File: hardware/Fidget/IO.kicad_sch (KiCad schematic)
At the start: 8 parts

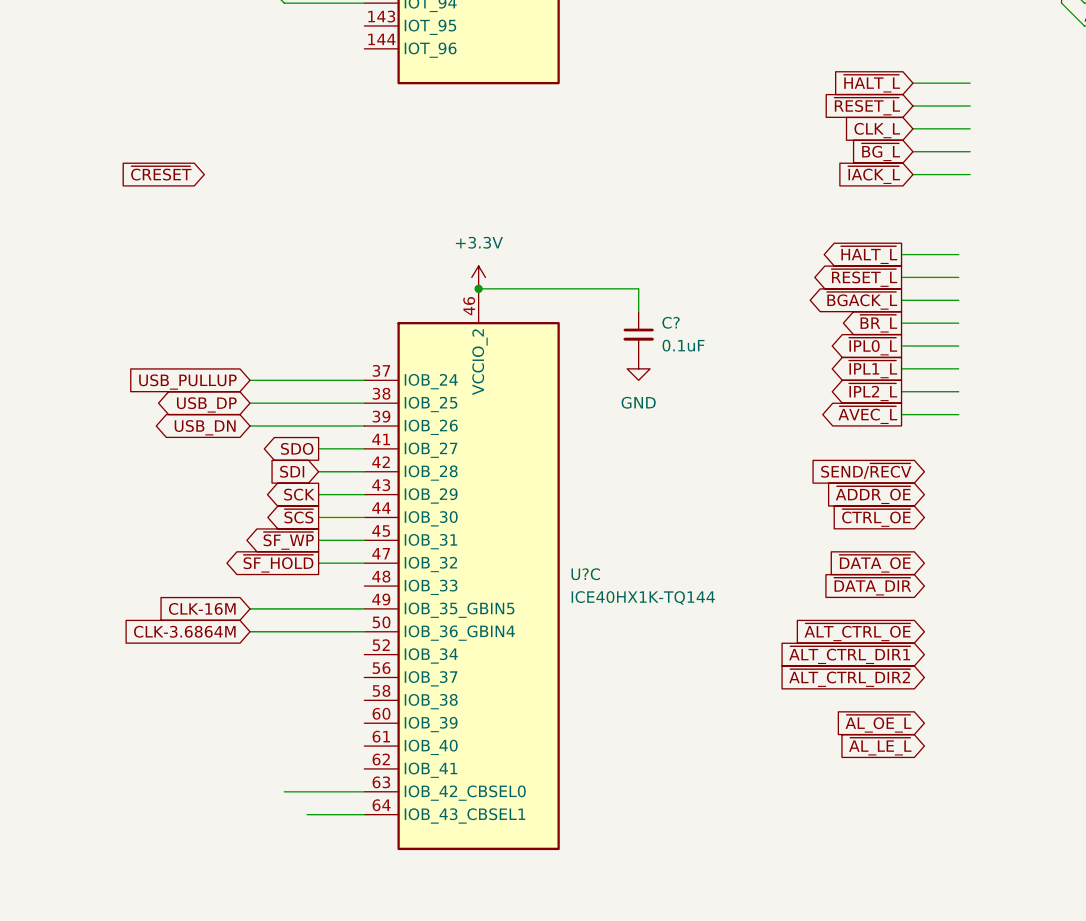
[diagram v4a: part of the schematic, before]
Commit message: Filled in more details in schematic
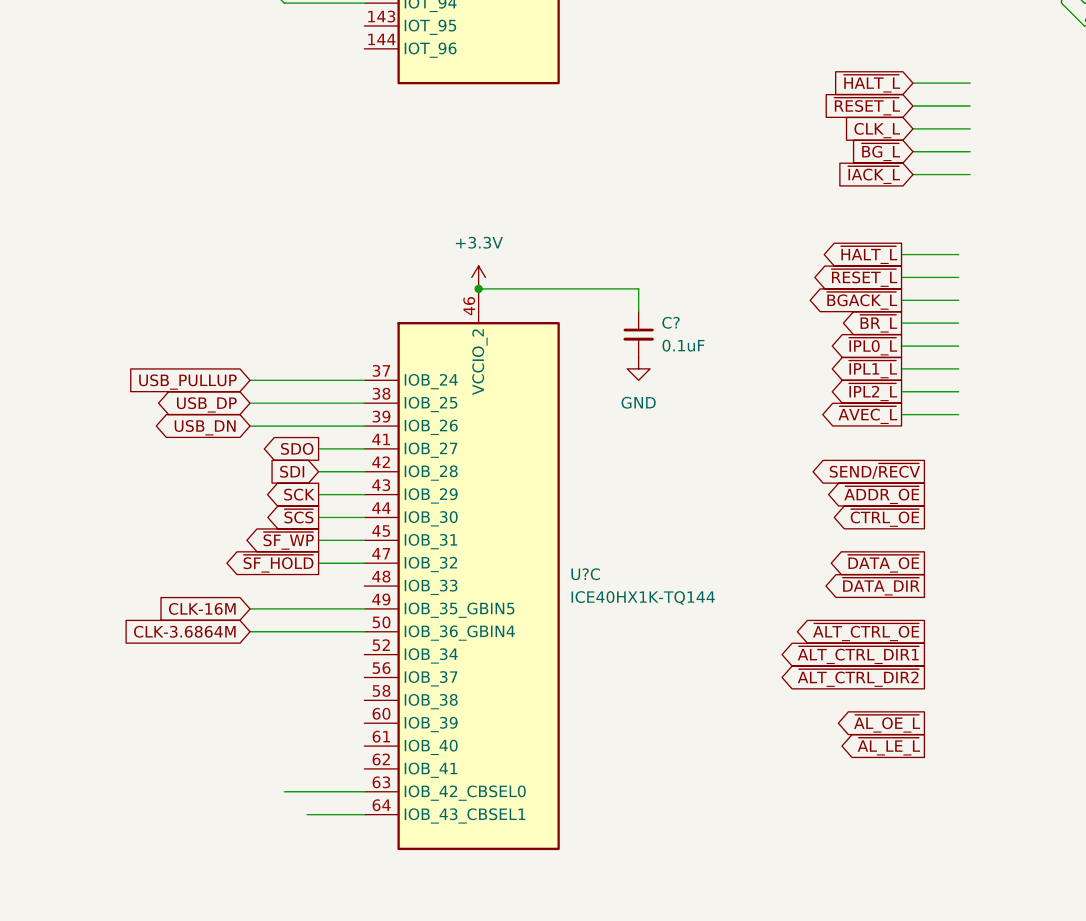
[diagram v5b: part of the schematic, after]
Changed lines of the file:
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@@
     (effects (font (size 1.27 1.27)) (justify left bottom))
   )
-  (global_label "~{DATA_DIR}" (shape input) (at 116.84 149.86 180) (fields_autoplaced)
+  (global_label "~{DATA_DIR}" (shape output) (at 116.84 149.86 180) (fields_autoplaced)
     (effects (font (size 1.27 1.27)) (justify right))
     (property "Intersheet References" "${INTERSHEET_REFS}" (id 0) (at 105.8998 149.7806 0)
@@
     )
   )
-  (global_label "~{AL_OE_L}" (shape input) (at 116.84 165.1 180) (fields_autoplaced)
+  (global_label "~{AL_OE_L}" (shape output) (at 116.84 165.1 180) (fields_autoplaced)
     (effects (font (size 1.27 1.27)) (justify right))
     (property "Intersheet References" "${INTERSHEET_REFS}" (id 0) (at 106.8674 165.0206 0)
@@
     )
   )
-  (global_label "~{DATA_OE}" (shape input) (at 116.84 147.32 180) (fields_autoplaced)
+  (global_label "~{DATA_OE}" (shape output) (at 116.84 147.32 180) (fields_autoplaced)
     (effects (font (size 1.27 1.27)) (justify right))
     (property "Intersheet References" "${INTERSHEET_REFS}" (id 0) (at 106.565 147.2406 0)
@@
     )
   )
-  (global_label "~{ALT_CTRL_DIR2}" (shape input) (at 116.84 160.02 180) (fields_autoplaced)
+  (global_label "~{ALT_CTRL_DIR2}" (shape output) (at 116.84 160.02 180) (fields_autoplaced)
     (effects (font (size 1.27 1.27)) (justify right))
     (property "Intersheet References" "${INTERSHEET_REFS}" (id 0) (at 100.5174 159.9406 0)
@@
     )
   )
-  (global_label "~{CRESET}" (shape input) (at 36.83 104.14 180) (fields_autoplaced)
-    (effects (font (size 1.27 1.27)) (justify right))
-    (property "Intersheet References" "${INTERSHEET_REFS}" (id 0) (at 27.4017 104.0606 0)
-      (effects (font (size 1.27 1.27)) (justify right) hide)
-    )
-  )
   (global_label "~{DS_L}" (shape input) (at 114.3 55.88 180) (fields_autoplaced)
     (effects (font (size 1.27 1.27)) (justify right))
@@
     )
   )
-  (global_label "~{ALT_CTRL_DIR1}" (shape input) (at 116.84 157.48 180) (fields_autoplaced)
+  (global_label "~{ALT_CTRL_DIR1}" (shape output) (at 116.84 157.48 180) (fields_autoplaced)
     (effects (font (size 1.27 1.27)) (justify right))
     (property "Intersheet References" "${INTERSHEET_REFS}" (id 0) (at 100.5174 157.4006 0)
@@
     )
   )
-  (global_label "~{AL_LE_L}" (shape input) (at 116.84 167.64 180) (fields_autoplaced)
+  (global_label "~{AL_LE_L}" (shape output) (at 116.84 167.64 180) (fields_autoplaced)
     (effects (font (size 1.27 1.27)) (justify right))
     (property "Intersheet References" "${INTERSHEET_REFS}" (id 0) (at 107.1698 167.5606 0)
@@
     )
   )
-  (global_label "SEND{slash}~{RECV}" (shape input) (at 116.84 137.16 180) (fields_autoplaced)
+  (global_label "SEND{slash}~{RECV}" (shape output) (at 116.84 137.16 180) (fields_autoplaced)
     (effects (font (size 1.27 1.27)) (justify right))
     (property "Intersheet References" "${INTERSHEET_REFS}" (id 0) (at 103.3598 137.0806 0)
@@
     )
   )
-  (global_label "~{ADDR_OE}" (shape input) (at 116.84 139.7 180) (fields_autoplaced)
+  (global_label "~{ADDR_OE}" (shape output) (at 116.84 139.7 180) (fields_autoplaced)
     (effects (font (size 1.27 1.27)) (justify right))
     (property "Intersheet References" "${INTERSHEET_REFS}" (id 0) (at 106.0812 139.6206 0)
@@
     )
   )
-  (global_label "~{CTRL_OE}" (shape input) (at 116.84 142.24 180) (fields_autoplaced)
+  (global_label "~{CTRL_OE}" (shape output) (at 116.84 142.24 180) (fields_autoplaced)
     (effects (font (size 1.27 1.27)) (justify right))
     (property "Intersheet References" "${INTERSHEET_REFS}" (id 0) (at 106.444 142.1606 0)
@@
     )
   )
-  (global_label "~{ALT_CTRL_OE}" (shape input) (at 116.84 154.94 180) (fields_autoplaced)
+  (global_label "~{ALT_CTRL_OE}" (shape output) (at 116.84 154.94 180) (fields_autoplaced)
     (effects (font (size 1.27 1.27)) (justify right))
     (property "Intersheet References" "${INTERSHEET_REFS}" (id 0) (at 102.3921 154.8606 0)

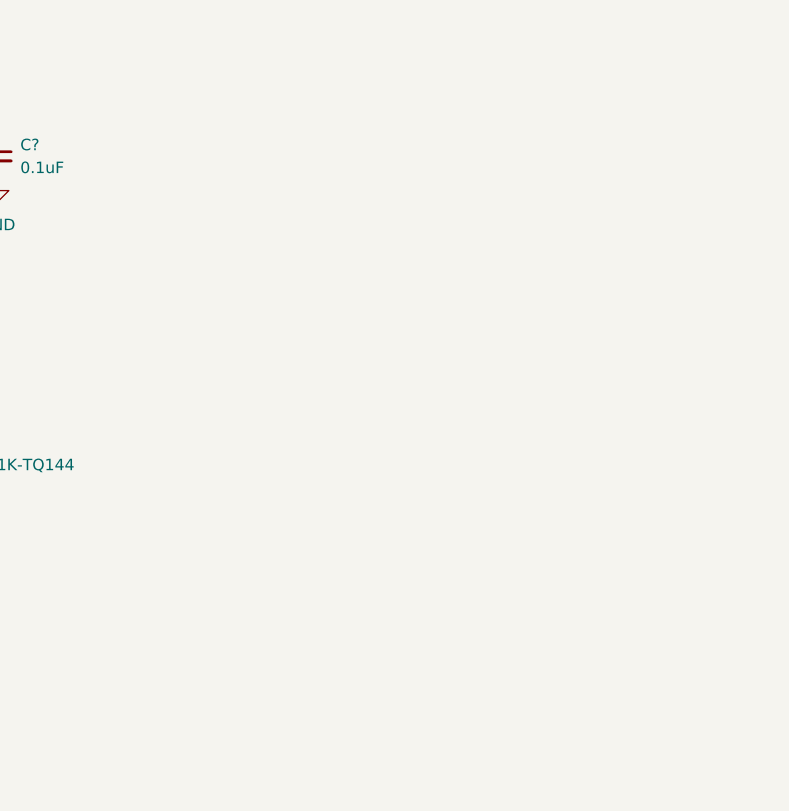
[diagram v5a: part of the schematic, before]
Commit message: Got simple RTL experiment of USART<->Bus in TinyFPGA
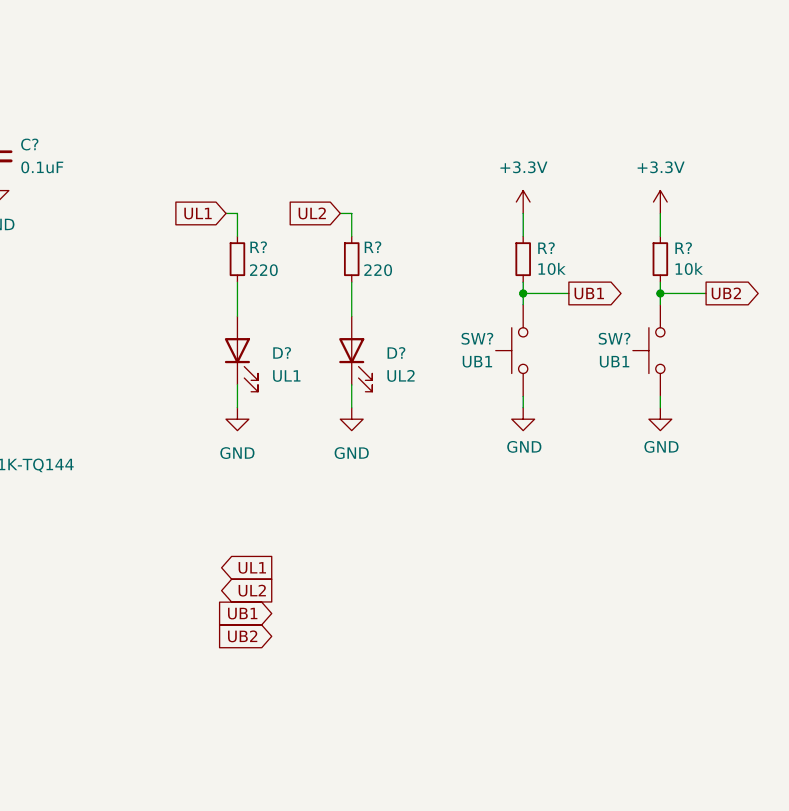
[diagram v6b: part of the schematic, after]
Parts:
- added D?: UL1, symbol Device:LED
- added D?: UL2, symbol Device:LED
- added R? (x2): 10k, Resistor_THT:R_Axial_DIN0204_L3.6mm_D1.6mm_P5.08mm_Horizontal, symbol Device:R_Small
- added R? (x2): 220, symbol Device:R_Small
- added SW? (x2): UB1, Button_Switch_THT:SW_PUSH_6mm, symbol Switch:SW_Push
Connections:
- net +3.3V: now also R?.1, R?.1
- net GND: now also D?.1 (K), D?.1 (K), SW?.1, SW?.1
- new net: D?.2 (A), R?.2 (x2)
- new net UB1: R?.2, SW?.2
- new net UB2: R?.2, SW?.2
- new net UL1: R?.1
- new net UL2: R?.1
